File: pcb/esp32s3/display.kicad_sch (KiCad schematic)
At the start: 5 parts, among them J5 Conn_01x40_Socket, Q3 DMG1012T

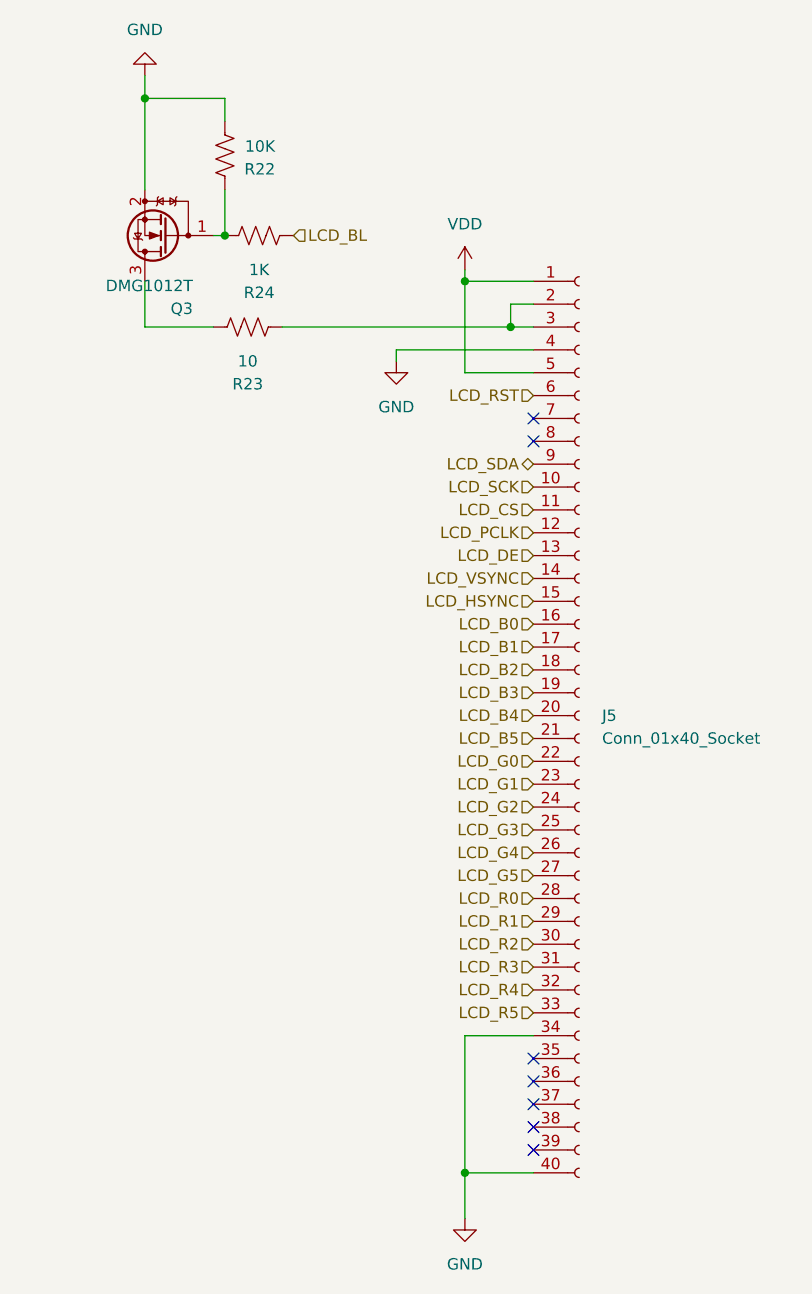
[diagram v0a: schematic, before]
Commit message: Update PCB with new components and footprints
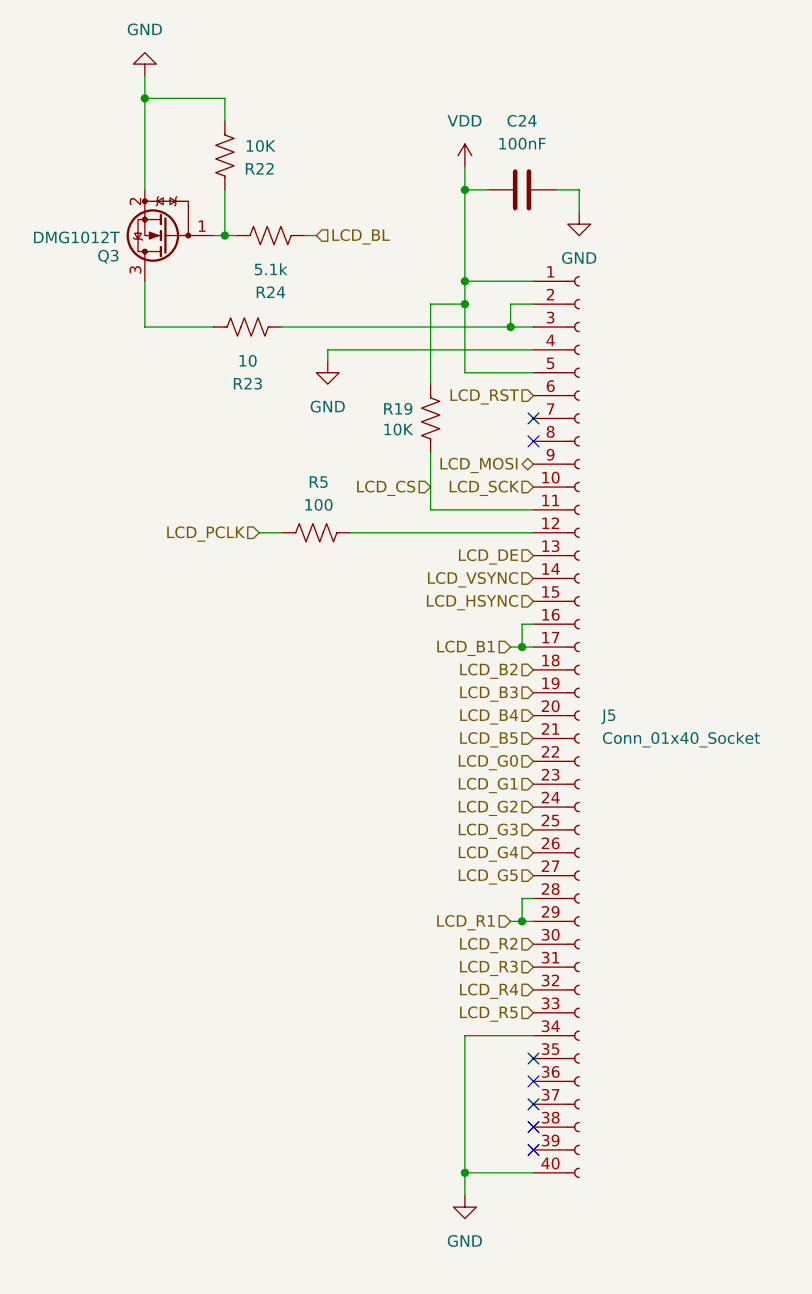
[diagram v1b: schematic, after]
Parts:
- added C24: 100nF, Capacitor_SMD:C_0402_1005Metric, symbol Device:C
- added R19: 10K, Resistor_SMD:R_0402_1005Metric, symbol Device:R_US
- added R5: 100, Resistor_SMD:R_0402_1005Metric, symbol Device:R_US
- R24: value 1K -> 5.1k
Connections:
- net LCD_B0 is gone; now on net LCD_B1: J5.16 (Pin_16)
- net LCD_R0 is gone; now on net LCD_R1: J5.28 (Pin_28)
- net GND: now also C24.2
- net LCD_CS: now also R19.1
- net LCD_PCLK: now also R5.1; no longer J5.12 (Pin_12)
- net VDD: now also C24.1, R19.2
- net LCD_SDA renamed LCD_MOSI
- new net: J5.12 (Pin_12), R5.2
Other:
- moved on the sheet: R24

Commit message: finishing touches
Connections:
- net VDD renamed +3V3
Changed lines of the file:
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@@
 			)
 		)
-		(property "Value" "VDD"
+		(property "Value" "+3V3"
 			(at 139.7 30.48 0)
 			(effects
